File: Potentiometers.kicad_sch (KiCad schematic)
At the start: 12 parts, among them J12 Conn_01x02, J7 Conn_01x03, J9 Conn_01x03

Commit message: fixed some footprints and part numbers
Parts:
- D2, D3: Mouser Part Number (none) -> 652-CDSOT23-T24CAN
- R13, R14: Mouser Part Number 71-CRCW080510K0FKEAC -> (none); P/N (none) -> Inventory
- R26: footprint (none) -> Resistor_SMD:R_0805_2012Metric; Mouser Part Number (none) -> 71-CRCW08051K00FKEAC
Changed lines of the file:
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@@
+			)
+		)
+		(property "Mouser Part Number" "652-CDSOT23-T24CAN"
+			(at 101.6 83.82 0)
+			(effects
+				(font
+					(size 1.27 1.27)
+				)
+				(hide yes)
 			)
 		)
@@
 			)
 		)
+		(property "Mouser Part Number" "652-CDSOT23-T24CAN"
+			(at 101.6 116.84 0)
+			(effects
+				(font
+					(size 1.27 1.27)
+				)
+				(hide yes)
+			)
+		)
 		(pin "2"
 		)
@@
 			)
 		)
+		(property "Mouser Part Number" "652-CDSOT23-T24CAN"
+			(at 101.6 74.93 0)
+			(effects
+				(font
+					(size 1.27 1.27)
+				)
+				(hide yes)
+			)
+		)
 		(pin "2"
 		)
@@
 			)
 		)
+		(property "Mouser Part Number" "652-CDSOT23-T24CAN"
+			(at 101.6 107.95 0)
+			(effects
+				(font
+					(size 1.27 1.27)
+				)
+				(hide yes)
+			)
+		)
 		(pin "2"
 		)
@@
 			)
 		)
-		(property "Mouser Part Number" "71-CRCW080510K0FKEAC "
+		(property "Mouser Part Number" ""
 			(at 92.71 104.14 0)
 			(effects
@@
 			)
 		)
+		(property "P/N" "Inventory"
+			(at 92.71 104.14 0)
+			(effects
+				(font
+					(size 1.27 1.27)
+				)
+				(hide yes)
+			)
+		)
 		(pin "1"
 		)
@@
 			)
 		)
-		(property "Mouser Part Number" "71-CRCW080510K0FKEAC "
+		(property "Mouser Part Number" ""
 			(at 93.98 83.82 0)
 			(effects
@@
 		)
 		(property "Vds" ""
+			(at 93.98 83.82 0)
+			(effects
+				(font
+					(size 1.27 1.27)
+				)
+				(hide yes)
+			)
+		)
+		(property "P/N" "Inventory"
 			(at 93.98 83.82 0)
 			(effects
@@
 			)
 		)
-		(property "Footprint" ""
+		(property "Footprint" "Resistor_SMD:R_0805_2012Metric"
 			(at 126.746 125.984 90)
 			(effects
@@
 			(at 125.73 125.73 0)
 			(effects
+				(font
+					(size 1.27 1.27)
+				)
+				(hide yes)
+			)
+		)
+		(property "Mouser Part Number" "71-CRCW08051K00FKEAC"
+			(at 125.73 125.73 0)
+			(effects

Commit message: Added/checked datasheet links/part numbers, deleted accel_pot2 and brake_pot2 hierarchical labels and changed corresponding pins (PC2, PC3) to GPIO on the now-2x5 extra GPIO connector.
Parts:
- C16, C17: Mouser Part Number 80-C0805C104K3R -> 80-C0805C104M5R
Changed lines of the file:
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@@
 			)
 		)
-		(property "Datasheet" "~"
+		(property "Datasheet" "https://www.mouser.com/ProductDetail/Bourns/CDSOT23-T24CAN?qs=Z7P4xsdcg2LuAOb%2FzQ7xoQ%3D%3D&srsltid=AfmBOoqcpMtelQv5uiWEJXHZOJjDhh8J7BlmNMXQdJmwOVQG7vUOPp-E"
 			(at 101.6 83.82 90)
 			(effects
@@
 			)
 		)
-		(property "Datasheet" "~"
+		(property "Datasheet" "https://www.mouser.com/ProductDetail/Bourns/CDSOT23-T24CAN?qs=Z7P4xsdcg2LuAOb%2FzQ7xoQ%3D%3D&srsltid=AfmBOoqcpMtelQv5uiWEJXHZOJjDhh8J7BlmNMXQdJmwOVQG7vUOPp-E"
 			(at 101.6 116.84 90)
 			(effects
@@
 			)
 		)
-		(property "Datasheet" "~"
+		(property "Datasheet" "https://www.mouser.com/ProductDetail/KEMET/C0805C104M5RACTU?qs=VOOUd%252Bza08qHu13WgNByHQ%3D%3D"
 			(at 83.82 83.82 0)
 			(effects
@@
 			)
 		)
-		(property "Mouser Part Number" "80-C0805C104K3R "
+		(property "Mouser Part Number" "80-C0805C104M5R"
 			(at 83.82 83.82 0)
 			(effects
@@
 			)
 		)
-		(property "Datasheet" "~"
+		(property "Datasheet" "https://www.mouser.in/ProductDetail/Vishay-Dale/CRCW080510K0FKEAC?qs=E3Y5ESvWgWORadmUijPtxQ%3D%3D"
 			(at 110.49 113.03 0)
 			(effects
@@
 			)
 		)
-		(property "Datasheet" "~"
+		(property "Datasheet" "https://www.mouser.com/ProductDetail/KEMET/C0805C104M5RACTU?qs=VOOUd%252Bza08qHu13WgNByHQ%3D%3D"
 			(at 83.82 116.84 0)
 			(effects
@@
 			)
 		)
-		(property "Mouser Part Number" "80-C0805C104K3R "
+		(property "Mouser Part Number" "80-C0805C104M5R"
 			(at 83.82 116.84 0)
 			(effects
@@
 			)
 		)
-		(property "Datasheet" "~"
+		(property "Datasheet" "https://www.mouser.com/ProductDetail/Bourns/CDSOT23-T24CAN?qs=Z7P4xsdcg2LuAOb%2FzQ7xoQ%3D%3D&srsltid=AfmBOoqcpMtelQv5uiWEJXHZOJjDhh8J7BlmNMXQdJmwOVQG7vUOPp-E"
 			(at 101.6 74.93 90)
 			(effects
@@
 			)
 		)
-		(property "Datasheet" "~"
+		(property "Datasheet" "https://www.mouser.com/ProductDetail/Bourns/CDSOT23-T24CAN?qs=Z7P4xsdcg2LuAOb%2FzQ7xoQ%3D%3D&srsltid=AfmBOoqcpMtelQv5uiWEJXHZOJjDhh8J7BlmNMXQdJmwOVQG7vUOPp-E"
 			(at 101.6 107.95 90)
 			(effects
@@
 			)
 		)
-		(property "Datasheet" "~"
+		(property "Datasheet" "https://www.mouser.in/ProductDetail/Vishay-Dale/CRCW080510K0FKEAC?qs=E3Y5ESvWgWORadmUijPtxQ%3D%3D"
 			(at 110.49 80.01 0)
 			(effects
@@
 			)
 		)
-		(property "Datasheet" "~"
+		(property "Datasheet" "https://www.mouser.com/ProductDetail/Vishay-Dale/CRCW08051K00FKEAC?qs=CZ6xfwOSLTXmQIgaYvN%2FBA%3D%3D"
 			(at 125.73 125.73 0)
 			(effects

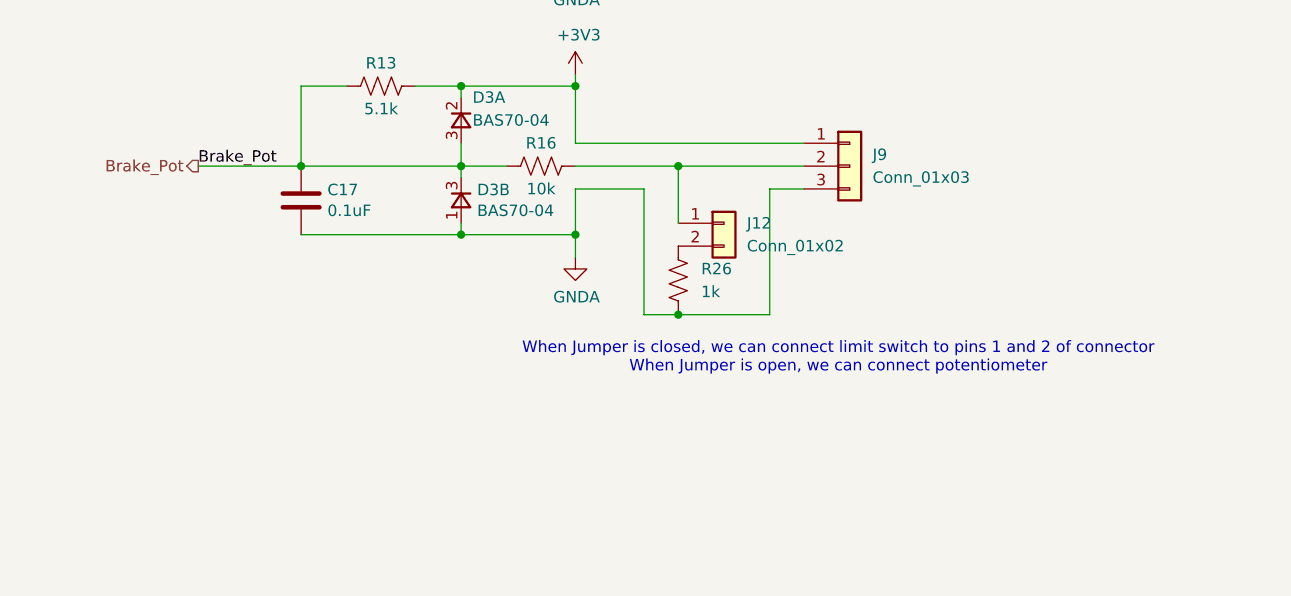
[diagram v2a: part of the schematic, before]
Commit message: added debouncing circuit for limit switch brake
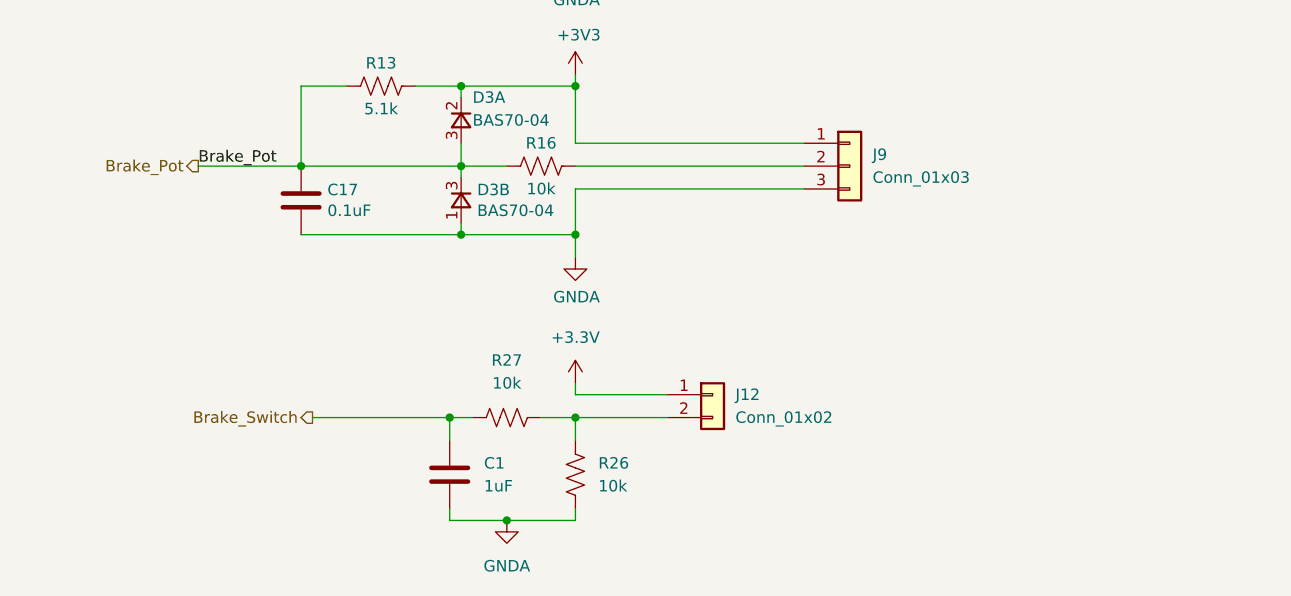
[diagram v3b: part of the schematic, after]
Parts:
- added C1: 1uF, Capacitor_SMD:C_0805_2012Metric, symbol Device:C
- added R27: 10k, Resistor_SMD:R_0805_2012Metric, symbol Device:R_US
- J12: footprint Connector_PinHeader_2.54mm:PinHeader_1x02_P2.54mm_Vertical -> Connector_Molex:Molex_Micro-Fit_3.0_43650-0215_1x02_P3.00mm_Vertical
- R26: value 1k -> 10k; Mouser Part Number 71-CRCW08051K00FKEAC -> 71-CRCW080510K0FKEAC
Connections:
- net GNDA: now also C1.2
- net at J9.2 (Pin_2), R16.1: no longer J12.1 (Pin_1)
- net at J12.2 (Pin_2), R26.1: now also R27.2
- new net +3.3V: J12.1 (Pin_1)
- new net Brake_Switch: C1.1, R27.1
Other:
- note removed: "When Jumper is closed, we can connect limit switch to pins 1 and 2 of connector When Jumper is open, we can connect potentiometer"

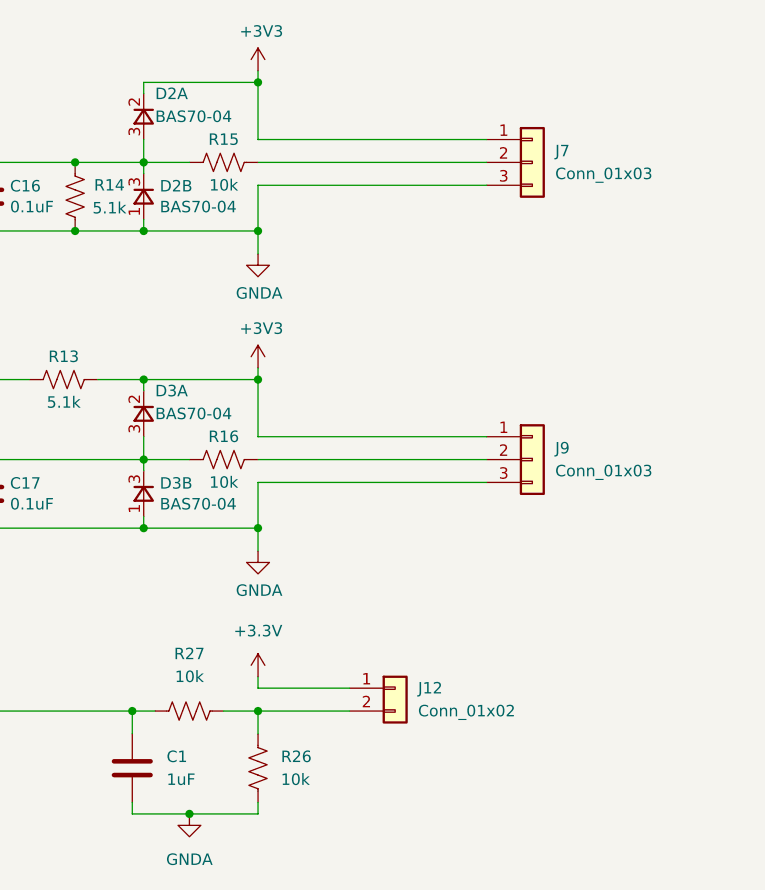
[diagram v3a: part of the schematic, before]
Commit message: Moved some things inward and squished board, added some labels, broke some traces up (sorry Krish 😣)
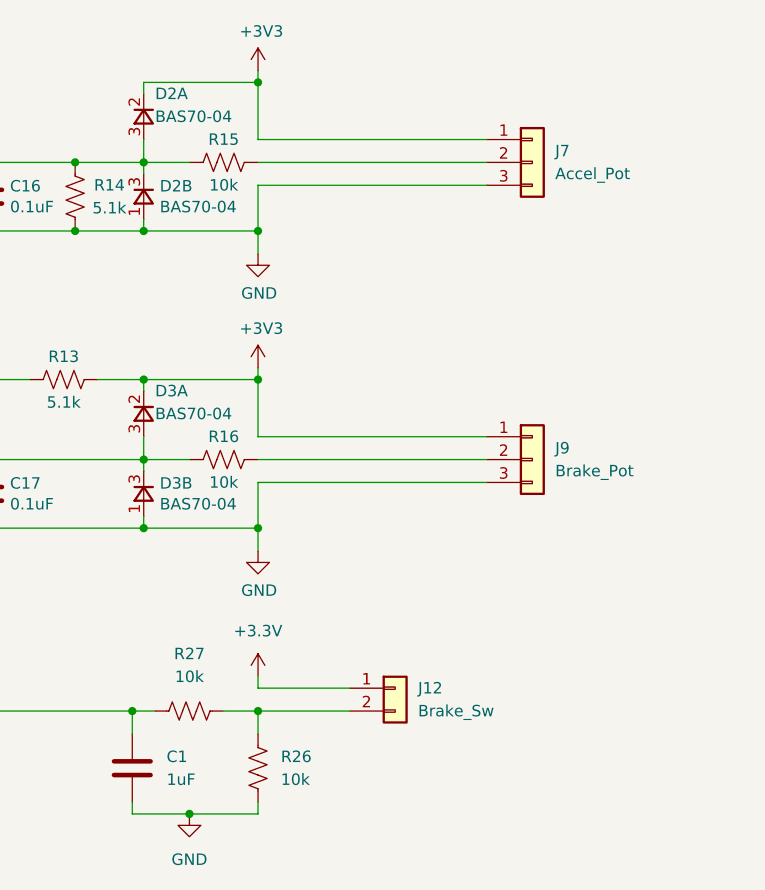
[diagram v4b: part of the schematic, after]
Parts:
- J12: value Conn_01x02 -> Brake_Sw
- J7: value Conn_01x03 -> Accel_Pot
- J9: value Conn_01x03 -> Brake_Pot
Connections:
- net GNDA renamed GND
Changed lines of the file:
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@@
 			)
 		)
-		(property "Value" "GNDA"
+		(property "Value" "GND"
 			(at 114.427 94.5642 0)
 			(effects
@@
 			)
 		)
-		(property "Value" "GNDA"
+		(property "Value" "GND"
 			(at 114.427 127.5842 0)
 			(effects
@@
 			)
 		)
-		(property "Value" "GNDA"
+		(property "Value" "GND"
 			(at 106.68 157.48 0)
 			(effects
@@
 			)
 		)
-		(property "Value" "Conn_01x02"
+		(property "Value" "Brake_Sw"
 			(at 132.08 140.9699 0)
 			(effects
@@
 			)
 		)
-		(property "Value" "Conn_01x03"
+		(property "Value" "Brake_Pot"
 			(at 147.32 114.2999 0)
 			(effects
@@
 			)
 		)
-		(property "Value" "Conn_01x03"
+		(property "Value" "Accel_Pot"
 			(at 147.32 81.2799 0)
 			(effects

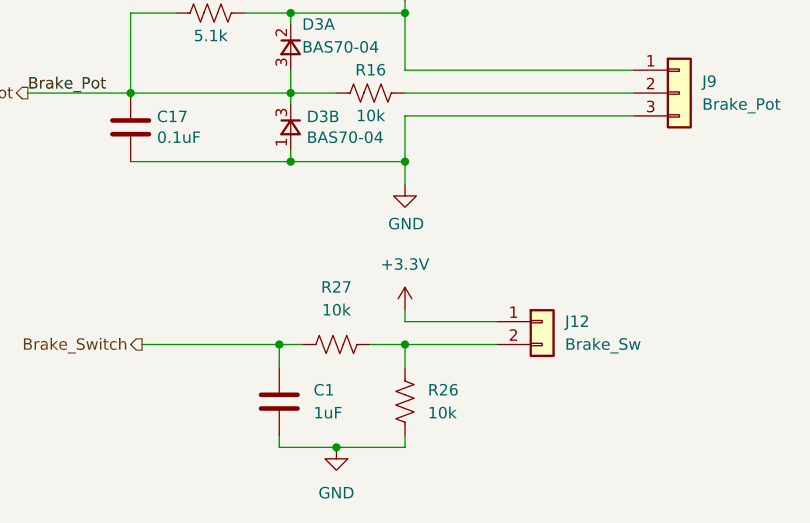
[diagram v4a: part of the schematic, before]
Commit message: routing is done other than power and usb, DRC is angry bc my goofy routing messed with a lot of the fills
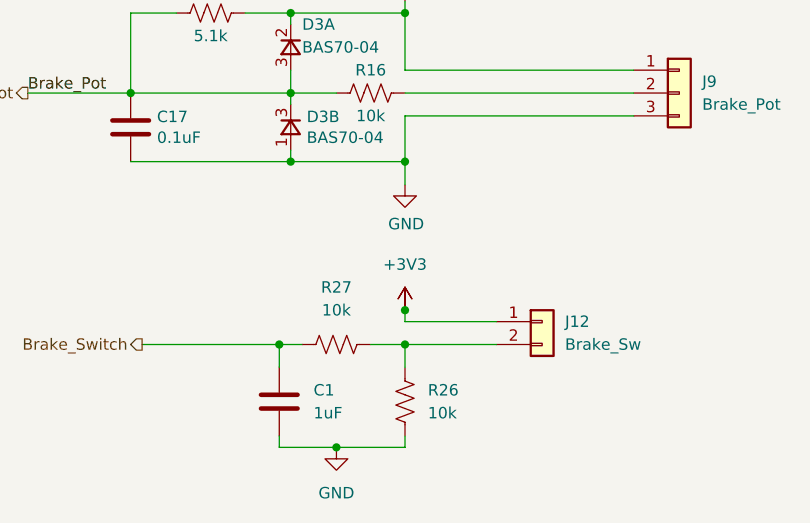
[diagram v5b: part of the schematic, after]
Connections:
- net +3V3 is gone; now on net +3.3V: D2.2, D3.2, J7.1 (Pin_1), J9.1 (Pin_1), R13.1
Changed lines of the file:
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@@
+	)
+	(junction
+		(at 114.3 137.16)
+		(diameter 0)
+		(color 0 0 0 0)
 	)
 	(junction
@@
 					(size 1.27 1.27)
 				)
+				(hide yes)
 			)
 		)
@@
 					(unit 1)
 				)
+			)
+		)
+	)
+	(symbol
+		(lib_id "power:+3V3")
+		(at 114.3 137.16 0)
+		(unit 1)
+		(exclude_from_sim no)
+		(in_bom yes)
+		(on_board yes)
+		(dnp no)
+		(fields_autoplaced yes)
+		(property "Reference" "#PWR01"
+			(at 114.3 140.97 0)
+			(effects
+				(font
+					(size 1.27 1.27)
+				)
+				(hide yes)
+			)
+		)
+		(property "Value" "+3V3"
+			(at 114.3 132.08 0)
+			(effects
+				(font
+					(size 1.27 1.27)
+				)
+			)
+		)
+		(property "Footprint" ""
+			(at 114.3 137.16 0)
+			(effects
+				(font
+					(size 1.27 1.27)
+				)
+				(hide yes)
+			)
+		)
+		(property "Datasheet" ""
+			(at 114.3 137.16 0)
+			(effects
+				(font
+					(size 1.27 1.27)
+				)
+				(hide yes)
+			)
+		)
+		(property "Description" "Power symbol creates a global label with name \"+3V3\""
+			(at 114.3 137.16 0)
+			(effects
+				(font
+					(size 1.27 1.27)
+				)
+				(hide yes)
+			)
+		)
+		(pin "1"
+		)
+		(instances
+			(project ""
+				(path "/66218487-e316-4467-9eba-79d4626ab24e/00000000-0000-0000-0000-00005fa99dc3"
+					(reference "#PWR01")
+					(unit 1)
+				)

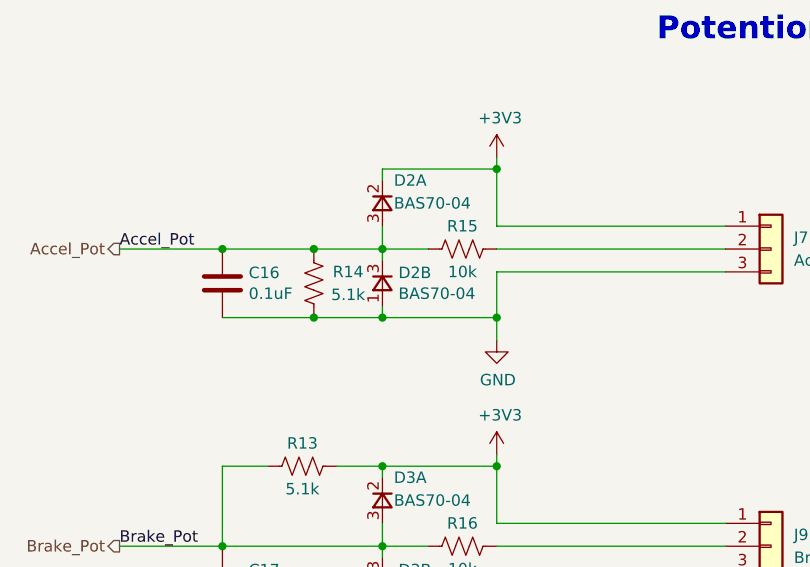
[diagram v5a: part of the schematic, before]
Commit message: Changed accel pot resistor values, did some layout aesthetic stuff, started on README.
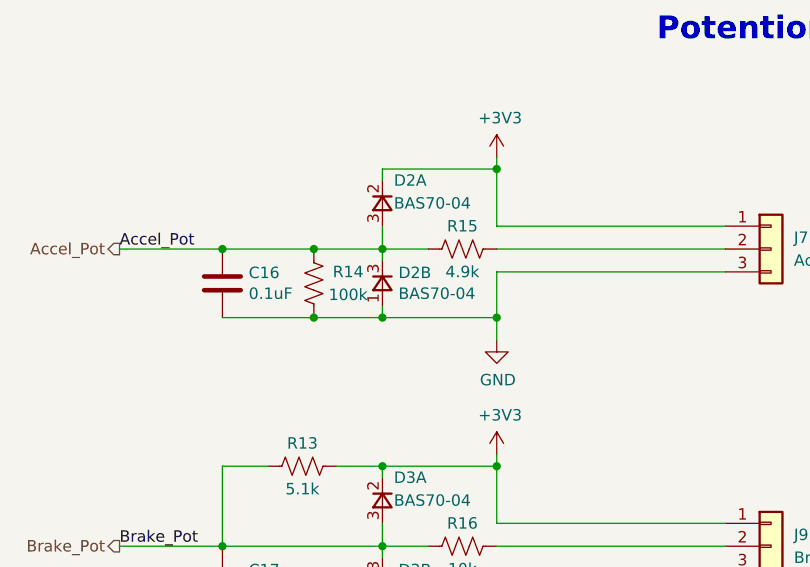
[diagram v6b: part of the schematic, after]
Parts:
- R14: value 5.1k -> 100k
- R15: value 10k -> 4.9k
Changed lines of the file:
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@@
 			)
 		)
-		(property "Value" "10k"
+		(property "Value" "4.9k"
 			(at 110.49 82.55 90)
 			(effects
@@
 			)
 		)
-		(property "Datasheet" "https://www.mouser.in/ProductDetail/Vishay-Dale/CRCW080510K0FKEAC?qs=E3Y5ESvWgWORadmUijPtxQ%3D%3D"
+		(property "Datasheet" "https://www.mouser.com/ProductDetail/Vishay-Dale/CRCW08054K99FKEAC?qs=E3Y5ESvWgWNlvFwCRtwMfw%3D%3D"
 			(at 110.49 80.01 0)
 			(effects
@@
 			)
 		)
-		(property "Value" "5.1k"
+		(property "Value" "100k"
 			(at 97.79 85.09 0)
 			(effects
@@
 			)
 		)
-		(property "Datasheet" "~"
+		(property "Datasheet" "https://www.mouser.in/ProductDetail/Vishay-Dale/CRCW0805100KFKEAC?qs=E3Y5ESvWgWORJvbAiaO1ug%3D%3D"
 			(at 93.98 83.82 0)
 			(effects
@@
 			)
 		)
-		(property "Datasheet" "~"
+		(property "Datasheet" "https://www.mouser.in/ProductDetail/Vishay-Dale/CRCW080510K0FKEAC?qs=E3Y5ESvWgWORadmUijPtxQ%3D%3D"
 			(at 114.3 147.32 0)
 			(effects
@@
 			)
 		)
-		(property "Datasheet" "~"
+		(property "Datasheet" "https://www.mouser.in/ProductDetail/Vishay-Dale/CRCW080510K0FKEAC?qs=E3Y5ESvWgWORadmUijPtxQ%3D%3D"
 			(at 106.68 140.97 0)
 			(effects

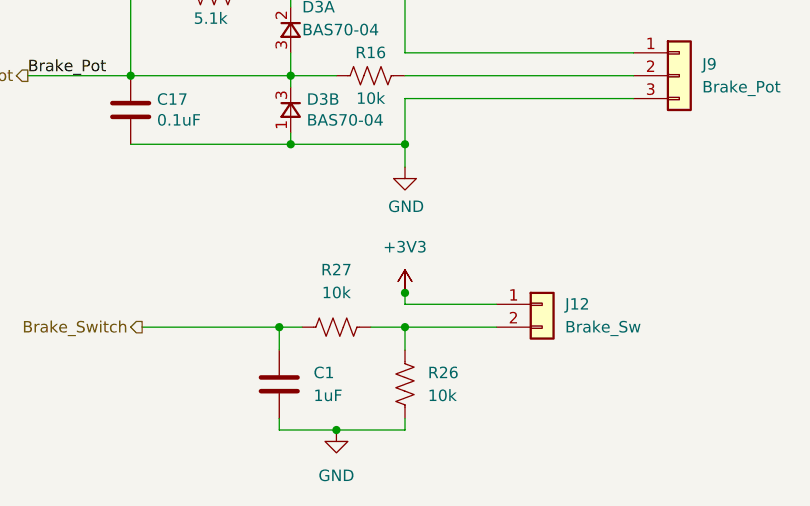
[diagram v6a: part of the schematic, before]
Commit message: Updated some symbols to use common libraries (and get rid of warnings.
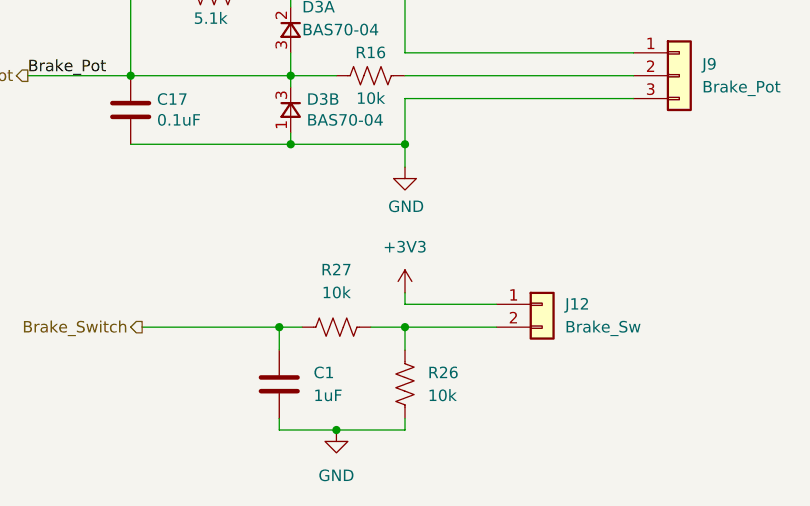
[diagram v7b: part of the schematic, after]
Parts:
- D2, D3: symbol Dashboard-rescue:BAS70-04-utsvt-chips -> utsvt-chips:BAS70-04
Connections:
- net +3.3V renamed +3V3
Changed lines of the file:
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@@
-	)
-	(junction
-		(at 114.3 137.16)
-		(diameter 0)
-		(color 0 0 0 0)
 	)
 	(junction
@@
 	)
 	(symbol
-		(lib_id "Dashboard-rescue:BAS70-04-utsvt-chips")
+		(lib_id "utsvt-chips:BAS70-04")
 		(at 101.6 83.82 270)
 		(unit 2)
@@
 	)
 	(symbol
-		(lib_id "Dashboard-rescue:BAS70-04-utsvt-chips")
+		(lib_id "utsvt-chips:BAS70-04")
 		(at 101.6 116.84 270)
 		(unit 2)
@@
 	)
 	(symbol
-		(lib_id "Dashboard-rescue:BAS70-04-utsvt-chips")
+		(lib_id "utsvt-chips:BAS70-04")
 		(at 101.6 74.93 270)
 		(unit 1)
@@
 	)
 	(symbol
-		(lib_id "Dashboard-rescue:BAS70-04-utsvt-chips")
+		(lib_id "utsvt-chips:BAS70-04")
 		(at 101.6 107.95 270)
 		(unit 1)
@@
 					(unit 1)
 				)
-			)
-		)
-	)
-	(symbol
-		(lib_id "power:+3.3V")
-		(at 114.3 137.16 0)
-		(unit 1)
-		(exclude_from_sim no)
-		(in_bom yes)
-		(on_board yes)
-		(dnp no)
-		(fields_autoplaced yes)
-		(property "Reference" "#PWR031"
-			(at 114.3 140.97 0)
-			(effects
-				(font
-					(size 1.27 1.27)
-				)
-				(hide yes)
-			)
-		)
-		(property "Value" "+3.3V"
-			(at 114.3 132.08 0)
-			(effects
-				(font
-					(size 1.27 1.27)
-				)
-				(hide yes)
-			)
-		)
-		(property "Footprint" ""
-			(at 114.3 137.16 0)
-			(effects
-				(font
-					(size 1.27 1.27)
-				)
-				(hide yes)
-			)
-		)
-		(property "Datasheet" ""
-			(at 114.3 137.16 0)
-			(effects
-				(font
-					(size 1.27 1.27)
-				)
-				(hide yes)
-			)
-		)
-		(property "Description" "Power symbol creates a global label with name \"+3.3V\""
-			(at 114.3 137.16 0)
-			(effects
-				(font
-					(size 1.27 1.27)
-				)
-				(hide yes)
-			)
-		)
-		(pin "1"
-		)
-		(instances
-			(project ""
-				(path "/66218487-e316-4467-9eba-79d4626ab24e/00000000-0000-0000-0000-00005fa99dc3"
-					(reference "#PWR031")
-					(unit 1)
-				)
